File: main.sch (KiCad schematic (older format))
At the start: 5 parts, among them J1 USB_OTG, J4 Conn_01x02, J6 Conn_01x02, Q1 Q_PMOS_GSD

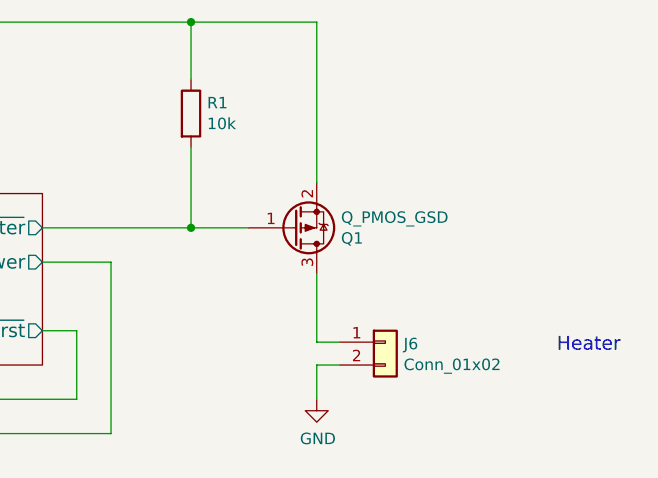
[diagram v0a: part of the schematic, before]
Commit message: Fixed NTLJF3117P MOSFET pin layout
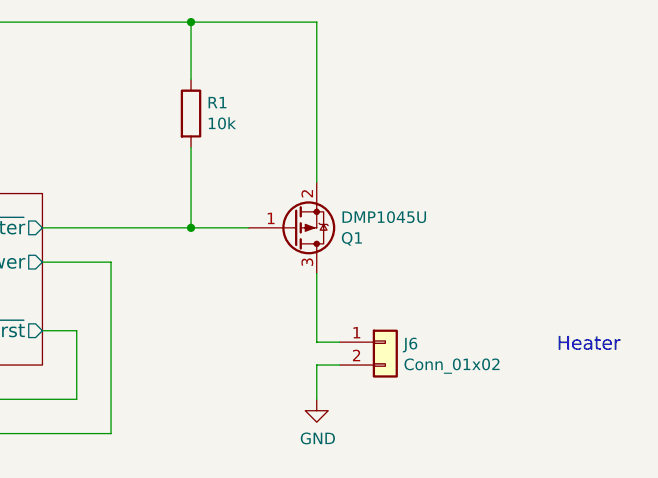
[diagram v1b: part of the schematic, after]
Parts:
- Q1: value Q_PMOS_GSD -> DMP1045U
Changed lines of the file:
@@
 P 7900 2850
 F 0 "Q1" H 8106 2896 50  0000 L CNN
-F 1 "Q_PMOS_GSD" H 8106 2805 50  0000 L CNN
+F 1 "DMP1045U" H 8106 2805 50  0000 L CNN
 F 2 "TO_SOT_Packages_SMD:SOT-23" H 8100 2950 50  0001 C CNN
 F 3 "" H 7900 2850 50  0001 C CNN

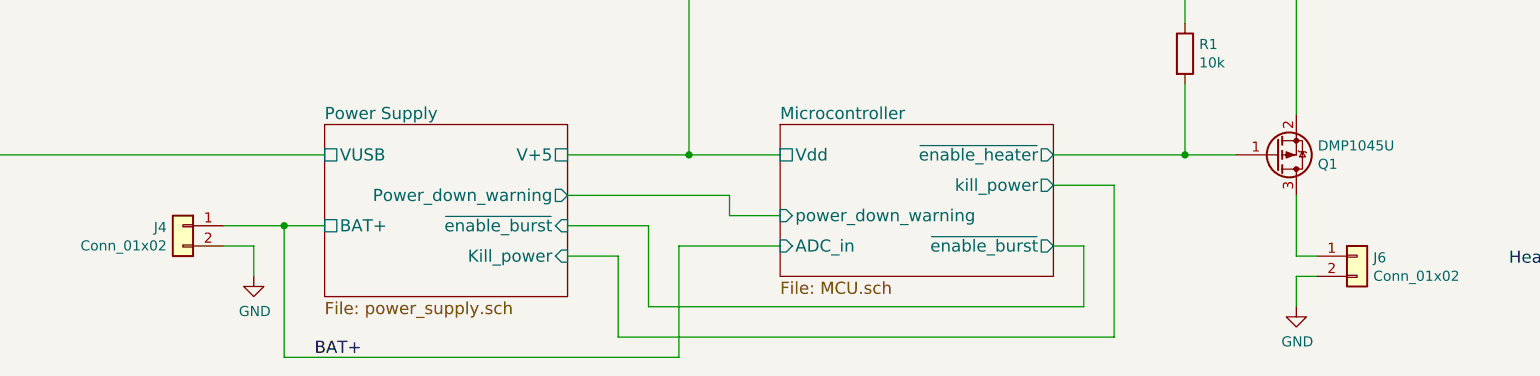
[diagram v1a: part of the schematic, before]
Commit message: Moved MCU pins around to make sure that they do not interfere with the programmer Moved ISP Header closer to the edge of the board to allow easier access with the programmer Added pulldown resistor to the DCD/DC converters enable pin to make sure it stays off in case of failure Added more PDFs of components
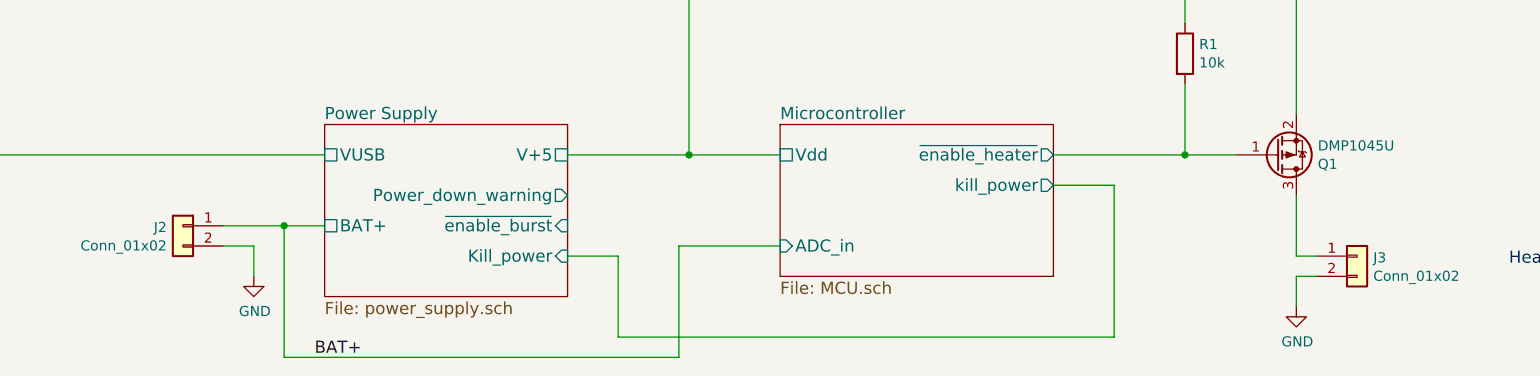
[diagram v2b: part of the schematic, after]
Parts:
- renumbered J4 to J2, J6 to J3
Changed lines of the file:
@@
 F4 "~enable_heater" O R 6800 2850 60
 F5 "kill_power" O R 6800 3000 60
-F6 "power_down_warning" I L 5450 3150 60
-F7 "~enable_burst" O R 6800 3300 60
 $EndSheet
 $Comp
@@
 NoConn ~ 1450 3250
 $Comp
-L Conn_01x02 J4
+L Conn_01x02 J2
 U 1 1 59D036F3
 P 2500 3200
-F 0 "J4" H 2580 3192 50  0000 L CNN
+F 0 "J2" H 2580 3192 50  0000 L CNN
 F 1 "Conn_01x02" H 2580 3101 50  0000 L CNN
 F 2 "Connectors_JST:JST_PH_B2B-PH-K_02x2.00mm_Straight" H 2500 3200 50  0001 C CNN
@@
 	4950 3300 5450 3300
 Connection ~ 3000 3200
-Wire Wire Line
-	4400 3050 5200 3050
-Wire Wire Line
-	5200 3050 5200 3150
-Wire Wire Line
-	5200 3150 5450 3150
 Wire Wire Line
 	6800 3000 7100 3000
@@
 	7450 2500 7450 2850
 Connection ~ 7450 2850
-Wire Wire Line
-	6800 3300 6950 3300
-Wire Wire Line
-	6950 3300 6950 3600
-Wire Wire Line
-	6950 3600 4800 3600
-Wire Wire Line
-	4800 3600 4800 3200
-Wire Wire Line
-	4800 3200 4400 3200
 $Comp
-L Conn_01x02 J6
+L Conn_01x02 J3
 U 1 1 59D13F2D
 P 8300 3350
-F 0 "J6" H 8380 3342 50  0000 L CNN
+F 0 "J3" H 8380 3342 50  0000 L CNN
 F 1 "Conn_01x02" H 8380 3251 50  0000 L CNN
 F 2 "Connectors_JST:JST_PH_B2B-PH-K_02x2.00mm_Straight" H 8300 3350 50  0001 C CNN

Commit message: Added part names and BOM Added Gerber files
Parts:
- J2, J3: MFN (none) -> JST; MFP (none) -> B2B-PH-K-S(LF)(SN)
- R1: MFN (none) -> Yageo; MFP (none) -> RC0603JR-0710KL
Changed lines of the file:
@@
 F 2 "Connectors_JST:JST_PH_B2B-PH-K_02x2.00mm_Straight" H 2500 3200 50  0001 C CNN
 F 3 "" H 2500 3200 50  0001 C CNN
+F 4 "JST" H 2500 3200 60  0001 C CNN "MFN"
+F 5 "B2B-PH-K-S(LF)(SN)" H 2500 3200 60  0001 C CNN "MFP"
 	1    2500 3200
 	-1   0    0    -1
@@
 F 2 "Resistors_SMD:R_0603" V 7380 2350 50  0001 C CNN
 F 3 "" H 7450 2350 50  0001 C CNN
+F 4 "Yageo" H 7450 2350 60  0001 C CNN "MFN"
+F 5 "RC0603JR-0710KL" H 7450 2350 60  0001 C CNN "MFP"
 	1    7450 2350
 	1    0    0    -1
@@
 F 2 "Connectors_JST:JST_PH_B2B-PH-K_02x2.00mm_Straight" H 8300 3350 50  0001 C CNN
 F 3 "" H 8300 3350 50  0001 C CNN
+F 4 "JST" H 8300 3350 60  0001 C CNN "MFN"
+F 5 "B2B-PH-K-S(LF)(SN)" H 8300 3350 60  0001 C CNN "MFP"
 	1    8300 3350
 	1    0    0    -1

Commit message: Preparing for v1.2 Updated to KiCAD 5 nightly Added resistors to isolate the programming pins Added transistor to drive the LED Replaced LTC3458 boost converter with an LTC3536 buck-boost converter to step down the USB power supply Added debugging jumper to test the voltage regulator
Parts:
- J1: symbol USB_OTG -> conn:USB_OTG
- J2, J3: symbol Conn_01x02 -> conn:Conn_01x02
- Q1: symbol Q_PMOS_GSD -> device:Q_PMOS_GSD
- R1: symbol R -> device:R
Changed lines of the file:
@@
-EESchema Schematic File Version 2
-LIBS:power
-LIBS:device
-LIBS:transistors
-LIBS:conn
-LIBS:linear
-LIBS:regul
-LIBS:74xx
-LIBS:cmos4000
-LIBS:adc-dac
-LIBS:memory
-LIBS:xilinx
-LIBS:microcontrollers
-LIBS:dsp
-LIBS:microchip
-LIBS:analog_switches
-LIBS:motorola
-LIBS:texas
-LIBS:intel
-LIBS:audio
-LIBS:interface
-LIBS:digital-audio
-LIBS:philips
-LIBS:display
-LIBS:cypress
-LIBS:siliconi
-LIBS:opto
-LIBS:atmel
-LIBS:contrib
-LIBS:valves
-LIBS:switches
-LIBS:Microchip
-LIBS:On Semiconductor
-LIBS:Linear Technology
+EESchema Schematic File Version 4
 LIBS:main-cache
 EELAYER 26 0
@@
 F3 "BAT+" U L 3200 3200 60
 F4 "V+5" U R 4400 2850 60
-F5 "Kill_power" I R 4400 3350 60
+F5 "~Kill_power" I R 4400 3350 60
 F6 "Power_down_warning" O R 4400 3050 60
 F7 "~enable_burst" I R 4400 3200 60
 $EndSheet
 $Comp
-L GND #PWR01
+L power:GND #PWR01
 U 1 1 59B6B421
 P 1150 3600
@@
 $EndComp
 Wire Wire Line
-	1150 3450 1150 3600
-$Comp
-L GND #PWR02
+	1150 3450 1150 3500
+$Comp
+L power:GND #PWR03
 U 1 1 59B6B5A0
 P 8000 3600
-F 0 "#PWR02" H 8000 3350 50  0001 C CNN
+F 0 "#PWR03" H 8000 3350 50  0001 C CNN
 F 1 "GND" H 8005 3427 50  0000 C CNN
 F 2 "" H 8000 3600 50  0001 C CNN
@@
 F3 "Vdd" U L 5450 2850 60
 F4 "~enable_heater" O R 6800 2850 60
-F5 "kill_power" O R 6800 3000 60
+F5 "~kill_power" O R 6800 3000 60
 $EndSheet
 $Comp
-L USB_OTG J1
+L conn:USB_OTG J1
 U 1 1 59CFD3FA
 P 1150 3050
@@
 NoConn ~ 1450 3250
 $Comp
-L Conn_01x02 J2
+L conn:Conn_01x02 J2
 U 1 1 59D036F3
 P 2500 3200
@@
 $EndComp
 Wire Wire Line
-	2700 3200 3200 3200
+	2700 3200 3000 3200
 Wire Wire Line
 	2700 3300 2850 3300
@@
 	2850 3300 2850 3450
 $Comp
-L GND #PWR03
+L power:GND #PWR02
 U 1 1 59D037E0
 P 2850 3450
-F 0 "#PWR03" H 2850 3200 50  0001 C CNN
+F 0 "#PWR02" H 2850 3200 50  0001 C CNN
 F 1 "GND" H 2855 3277 50  0000 C CNN
 F 2 "" H 2850 3450 50  0001 C CNN
@@
 $EndComp
 Wire Wire Line
-	4400 2850 5450 2850
+	4400 2850 5000 2850
 Wire Wire Line
 	3000 3200 3000 3850
@@
 	4650 3350 4400 3350
 $Comp
-L Q_PMOS_GSD Q1
+L device:Q_PMOS_GSD Q1
 U 1 1 59D0E0A3
 P 7900 2850
@@
 	8000 3050 8000 3350
 Wire Wire Line
-	6800 2850 7700 2850
+	6800 2850 7450 2850
 Wire Wire Line
 	5000 2850 5000 1950
 Wire Wire Line
-	5000 1950 8000 1950
+	5000 1950 7450 1950
 Wire Wire Line
 	8000 1950 8000 2650
 Connection ~ 5000 2850
 $Comp
-L R R1
+L device:R R1
 U 1 1 59D0E311
 P 7450 2350
@@
 Connection ~ 7450 2850
 $Comp
-L Conn_01x02 J3
+L conn:Conn_01x02 J3
 U 1 1 59D13F2D
 P 8300 3350
@@
 	1050 3500 1150 3500
 Connection ~ 1150 3500
+Wire Wire Line
+	3000 3200 3200 3200
+Wire Wire Line
+	5000 2850 5450 2850
+Wire Wire Line
+	7450 1950 8000 1950
+Wire Wire Line
+	7450 2850 7700 2850
+Wire Wire Line
+	1150 3500 1150 3600
 $EndSCHEMATC

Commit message: Updated to Kicad v5.0
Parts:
- added LOGO1: Logo_Open_Hardware_Small, Symbol:OSHW-Logo_7.5x8mm_SilkScreen, symbol Graphic:Logo_Open_Hardware_Small
- J1: value USB_OTG -> USB_MICRO; symbol conn:USB_OTG -> Connector:USB_B_Micro
- J2, J3: symbol conn:Conn_01x02 -> Connector_Generic:Conn_01x02
- Q1: symbol device:Q_PMOS_GSD -> Device:Q_PMOS_GSD
- R1: symbol device:R -> Device:R
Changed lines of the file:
@@
 $EndSheet
 $Comp
-L conn:USB_OTG J1
+L Connector:USB_B_Micro J1
 U 1 1 59CFD3FA
 P 1150 3050
 F 0 "J1" H 1205 3517 50  0000 C CNN
-F 1 "USB_OTG" H 1205 3426 50  0000 C CNN
+F 1 "USB_MICRO" H 1205 3426 50  0000 C CNN
 F 2 "Custom_footprints:USB_MICRO" H 1300 3000 50  0001 C CNN
 F 3 "" H 1300 3000 50  0001 C CNN
@@
 NoConn ~ 1450 3250
 $Comp
-L conn:Conn_01x02 J2
+L Connector_Generic:Conn_01x02 J2
 U 1 1 59D036F3
 P 2500 3200
@@
 	4650 3350 4400 3350
 $Comp
-L device:Q_PMOS_GSD Q1
+L Device:Q_PMOS_GSD Q1
 U 1 1 59D0E0A3
 P 7900 2850
@@
 Connection ~ 5000 2850
 $Comp
-L device:R R1
+L Device:R R1
 U 1 1 59D0E311
 P 7450 2350
@@
 Connection ~ 7450 2850
 $Comp
-L conn:Conn_01x02 J3
+L Connector_Generic:Conn_01x02 J3
 U 1 1 59D13F2D
 P 8300 3350
@@
 Wire Wire Line
 	1150 3500 1150 3600
+$Comp
+L Graphic:Logo_Open_Hardware_Small LOGO1
+U 1 1 5B09E787
+P 9750 5400
+F 0 "LOGO1" H 9750 5675 50  0001 C CNN
+F 1 "Logo_Open_Hardware_Small" H 9750 5175 50  0001 C CNN
+F 2 "Symbol:OSHW-Logo_7.5x8mm_SilkScreen" H 9750 5400 50  0001 C CNN
+F 3 "~" H 9750 5400 50  0001 C CNN
+	1    9750 5400
+	1    0    0    -1
+$EndComp
 $EndSCHEMATC

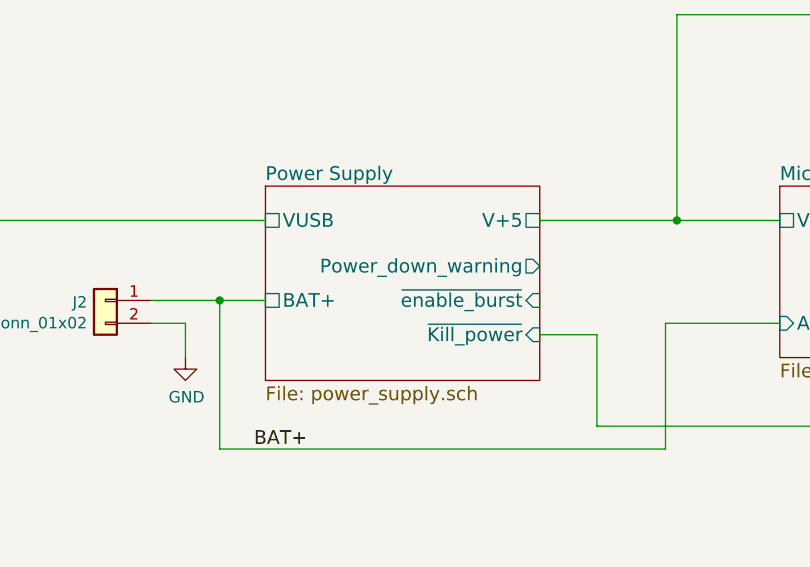
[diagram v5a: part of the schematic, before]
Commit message: Added power on state LED Updated to KiCAD 5.0
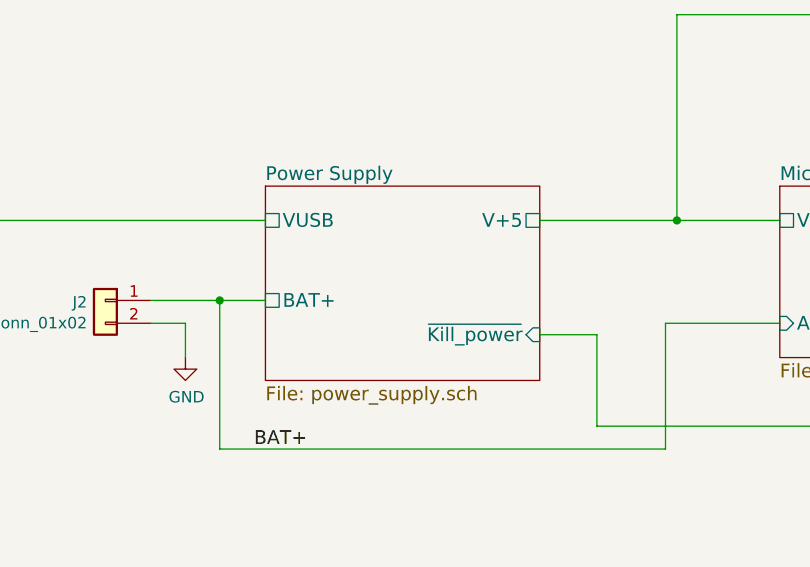
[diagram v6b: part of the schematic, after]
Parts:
- Q1: footprint TO_SOT_Packages_SMD:SOT-23 -> Package_TO_SOT_SMD:SOT-23
- R1: footprint Resistors_SMD:R_0603 -> Resistor_SMD:R_0603_1608Metric
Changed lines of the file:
@@
 F4 "V+5" U R 4400 2850 60
 F5 "~Kill_power" I R 4400 3350 60
-F6 "Power_down_warning" O R 4400 3050 60
-F7 "~enable_burst" I R 4400 3200 60
 $EndSheet
 $Comp
@@
 F 0 "Q1" H 8106 2896 50  0000 L CNN
 F 1 "DMP1045U" H 8106 2805 50  0000 L CNN
-F 2 "TO_SOT_Packages_SMD:SOT-23" H 8100 2950 50  0001 C CNN
+F 2 "Package_TO_SOT_SMD:SOT-23" H 8100 2950 50  0001 C CNN
 F 3 "" H 7900 2850 50  0001 C CNN
 F 4 "Diodes Inc." H 7900 2850 60  0001 C CNN "MFN"
@@
 F 0 "R1" H 7520 2396 50  0000 L CNN
 F 1 "10k" H 7520 2305 50  0000 L CNN
-F 2 "Resistors_SMD:R_0603" V 7380 2350 50  0001 C CNN
+F 2 "Resistor_SMD:R_0603_1608Metric" V 7380 2350 50  0001 C CNN
 F 3 "" H 7450 2350 50  0001 C CNN
 F 4 "Yageo" H 7450 2350 60  0001 C CNN "MFN"
